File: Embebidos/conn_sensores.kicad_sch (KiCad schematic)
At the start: 3 parts, among them J5 Conn_01x04, J6 Conn_02x06_Counter_Clockwise, J7 Conn_01x08

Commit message: organizando
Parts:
- added J8: Conn_01x02, Connector_JST:JST_EH_S2B-EH_1x02_P2.50mm_Horizontal, symbol Connector_Generic:Conn_01x02
- J6: renamed from J7; footprint Connector_PinHeader_2.54mm:PinHeader_1x08_P2.54mm_Vertical -> Connector_JST:JST_EH_S8B-EH_1x08_P2.50mm_Horizontal
- J7: renamed from J5; footprint Connector_PinHeader_2.54mm:PinHeader_1x04_P2.54mm_Vertical -> Connector_JST:JST_EH_B4B-EH-A_1x04_P2.50mm_Vertical
- renumbered J6 to J5
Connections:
- net GND: now also J8.2 (Pin_2)
- new net +5V: J8.1 (Pin_1)
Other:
- moved on the sheet: J6, J7

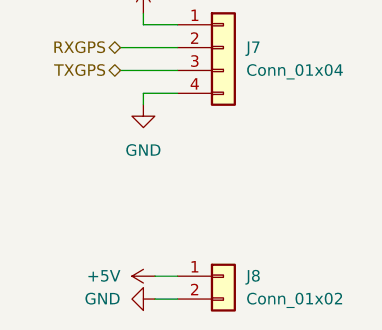
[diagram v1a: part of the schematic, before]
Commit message: mas orden en la ubicacion de huellas
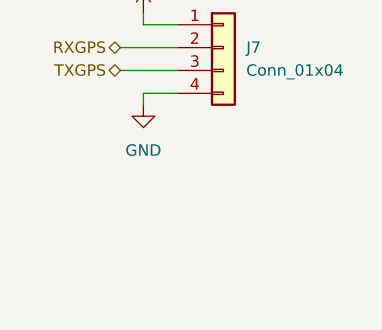
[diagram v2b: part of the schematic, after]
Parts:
- removed J8: Conn_01x02, Connector_JST:JST_EH_S2B-EH_1x02_P2.50mm_Horizontal, symbol Connector_Generic:Conn_01x02
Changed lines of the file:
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@@
-    (stroke (width 0) (type default) (color 0 0 0 0))
-  )
-  (wire (pts (xy 90.17 119.38) (xy 92.71 119.38))
     (stroke (width 0) (type default) (color 0 0 0 0))
   )
@@
   )
   (wire (pts (xy 88.9 88.9) (xy 88.9 87.63))
-    (stroke (width 0) (type default) (color 0 0 0 0))
-  )
-  (wire (pts (xy 90.17 116.84) (xy 92.71 116.84))
     (stroke (width 0) (type default) (color 0 0 0 0))
   )
@@
   (symbol (lib_id "power:GND") (at 83.82 39.37 270) (unit 1)
     (in_bom yes) (on_board yes)
-    (property "Reference" "#PWR044" (id 0) (at 77.47 39.37 0)
+    (property "Reference" "#PWR046" (id 0) (at 77.47 39.37 0)
       (effects (font (size 1.27 1.27)) hide)
     )
@@
     (pin "9")
   )
-  (symbol (lib_id "power:+5V") (at 90.17 116.84 90) (unit 1)
-    (in_bom yes) (on_board yes) (fields_autoplaced)
-    (property "Reference" "#PWR047" (id 0) (at 93.98 116.84 0)
-      (effects (font (size 1.27 1.27)) hide)
-    )
-    (property "Value" "+5V" (id 1) (at 86.36 116.8399 90)
-      (effects (font (size 1.27 1.27)) (justify left))
-    )
-    (property "Footprint" "" (id 2) (at 90.17 116.84 0)
-      (effects (font (size 1.27 1.27)) hide)
-    )
-    (property "Datasheet" "" (id 3) (at 90.17 116.84 0)
-      (effects (font (size 1.27 1.27)) hide)
-    )
-    (pin "1")
-  )
   (symbol (lib_id "Connector_Generic:Conn_01x04") (at 97.79 91.44 0) (unit 1)
     (in_bom yes) (on_board yes) (fields_autoplaced)
@@
     (pin "4")
   )
-  (symbol (lib_id "Connector_Generic:Conn_01x02") (at 97.79 116.84 0) (unit 1)
-    (in_bom yes) (on_board yes) (fields_autoplaced)
-    (property "Reference" "J8" (id 0) (at 100.33 116.8399 0)
-      (effects (font (size 1.27 1.27)) (justify left))
-    )
-    (property "Value" "Conn_01x02" (id 1) (at 100.33 119.3799 0)
-      (effects (font (size 1.27 1.27)) (justify left))
-    )
-    (property "Footprint" "Connector_JST:JST_EH_S2B-EH_1x02_P2.50mm_Horizontal" (id 2) (at 97.79 116.84 0)
-      (effects (font (size 1.27 1.27)) hide)
-    )
-    (property "Datasheet" "~" (id 3) (at 97.79 116.84 0)
-      (effects (font (size 1.27 1.27)) hide)
-    )
-    (pin "1")
-    (pin "2")
-  )
   (symbol (lib_id "power:GND") (at 88.9 97.79 0) (unit 1)
     (in_bom yes) (on_board yes) (fields_autoplaced)
-    (property "Reference" "#PWR046" (id 0) (at 88.9 104.14 0)
+    (property "Reference" "#PWR048" (id 0) (at 88.9 104.14 0)
       (effects (font (size 1.27 1.27)) hide)
     )
@@
   (symbol (lib_id "power:+3.3V") (at 88.9 87.63 0) (unit 1)
     (in_bom yes) (on_board yes)
-    (property "Reference" "#PWR045" (id 0) (at 88.9 91.44 0)
+    (property "Reference" "#PWR047" (id 0) (at 88.9 91.44 0)
       (effects (font (size 1.27 1.27)) hide)
     )
@@
       (effects (font (size 1.27 1.27)) hide)
     )
-    (pin "1")
-  )
-  (symbol (lib_id "power:GND") (at 90.17 119.38 270) (unit 1)
-    (in_bom yes) (on_board yes) (fields_autoplaced)
-    (property "Reference" "#PWR048" (id 0) (at 83.82 119.38 0)
-      (effects (font (size 1.27 1.27)) hide)
-    )
-    (property "Value" "GND" (id 1) (at 86.36 119.3799 90)
-      (effects (font (size 1.27 1.27)) (justify right))
-    )
-    (property "Footprint" "" (id 2) (at 90.17 119.38 0)
-      (effects (font (size 1.27 1.27)) hide)
-    )
-    (property "Datasheet" "" (id 3) (at 90.17 119.38 0)
-      (effects (font (size 1.27 1.27)) hide)
-    )
